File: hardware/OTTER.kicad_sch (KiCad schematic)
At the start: 0 parts

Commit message: starting layout
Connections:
- no-connect marks 15 -> 16
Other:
- sheet PMOD Connector ports: added JA4; removed none
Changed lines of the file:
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@@
+	)
+	(no_connect
+		(at 97.79 73.66)
 	)
 	(no_connect
@@
 	(wire
 		(pts
-			(xy 139.7 27.94) (xy 157.48 27.94)
+			(xy 78.74 39.37) (xy 93.98 39.37)
 		)
 		(stroke
@@
 	(wire
 		(pts
-			(xy 78.74 39.37) (xy 93.98 39.37)
+			(xy 78.74 48.26) (xy 93.98 48.26)
 		)
 		(stroke
@@
 	(wire
 		(pts
-			(xy 78.74 48.26) (xy 93.98 48.26)
+			(xy 139.7 30.48) (xy 157.48 30.48)
 		)
 		(stroke
@@
 	(wire
 		(pts
-			(xy 139.7 30.48) (xy 157.48 30.48)
+			(xy 78.74 29.21) (xy 93.98 29.21)
 		)
 		(stroke
@@
 	(wire
 		(pts
-			(xy 78.74 29.21) (xy 93.98 29.21)
+			(xy 139.7 35.56) (xy 157.48 35.56)
 		)
 		(stroke
@@
 	(wire
 		(pts
-			(xy 139.7 35.56) (xy 157.48 35.56)
+			(xy 78.74 53.34) (xy 93.98 53.34)
 		)
 		(stroke
@@
 	(wire
 		(pts
-			(xy 78.74 53.34) (xy 93.98 53.34)
+			(xy 78.74 31.75) (xy 93.98 31.75)
 		)
 		(stroke
@@
 	(wire
 		(pts
-			(xy 78.74 31.75) (xy 93.98 31.75)
+			(xy 139.7 38.1) (xy 157.48 38.1)
 		)
 		(stroke
@@
 	(wire
 		(pts
-			(xy 139.7 38.1) (xy 157.48 38.1)
+			(xy 78.74 55.88) (xy 93.98 55.88)
 		)
 		(stroke
@@
 	(wire
 		(pts
-			(xy 78.74 55.88) (xy 93.98 55.88)
+			(xy 78.74 34.29) (xy 93.98 34.29)
 		)
 		(stroke
@@
 	(wire
 		(pts
-			(xy 78.74 34.29) (xy 93.98 34.29)
+			(xy 78.74 36.83) (xy 93.98 36.83)
 		)
 		(stroke
@@
 	(wire
 		(pts
-			(xy 78.74 36.83) (xy 93.98 36.83)
+			(xy 78.74 44.45) (xy 93.98 44.45)
 		)
 		(stroke
@@
 	(wire
 		(pts
-			(xy 78.74 44.45) (xy 93.98 44.45)
+			(xy 139.7 33.02) (xy 157.48 33.02)
 		)
 		(stroke
@@
 	(wire
 		(pts
-			(xy 139.7 33.02) (xy 157.48 33.02)
+			(xy 139.7 40.64) (xy 157.48 40.64)
 		)
 		(stroke
@@
 		)
 		(pin "JD1" output
-			(at 139.7 27.94 0)
+			(at 139.7 40.64 0)
 			(effects
 				(font
@@
 		(pin "JD9" output
 			(at 93.98 31.75 180)
+			(effects
+				(font
+					(size 1.27 1.27)
+				)
+				(justify left)
+			)
+		)
+		(pin "JA4" output
+			(at 97.79 73.66 270)
 			(effects
 				(font
@@
 		)
 		(pin "CS" input
-			(at 157.48 27.94 180)
-			(effects
-				(font
+			(at 157.48 40.64 180)
+			(effects
+				(font

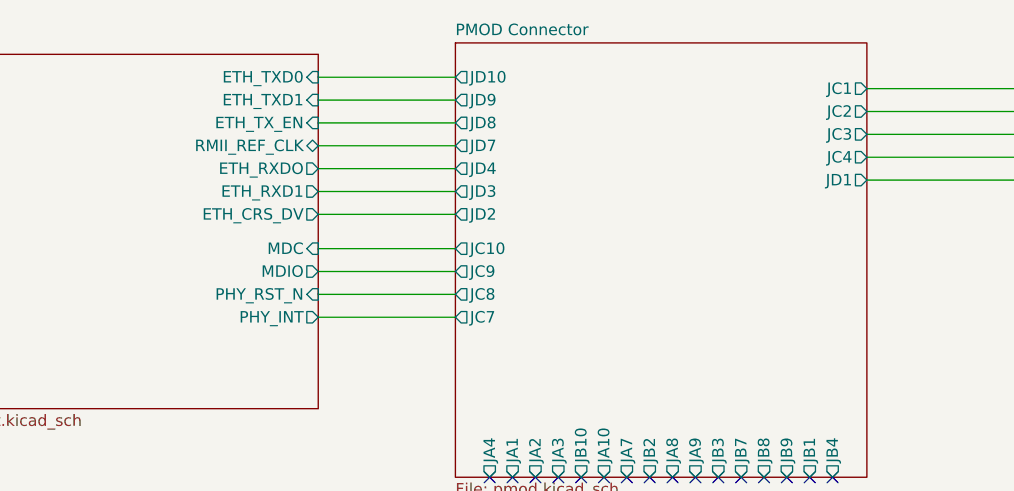
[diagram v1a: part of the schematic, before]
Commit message: changed pinout to match trs-star. also added resistors for spi
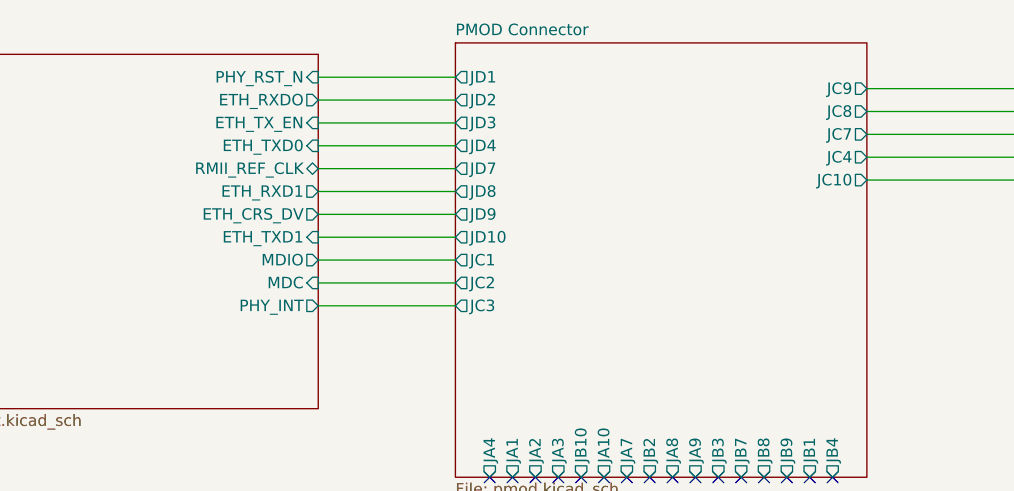
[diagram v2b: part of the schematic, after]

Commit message: most of layout is done, only have single ended highspeed signals left. mika pleaaaaaaaaaaaaaaaaaseeeeeeee review :beg:
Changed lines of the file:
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@@
-	(wire
-		(pts
-			(xy 139.7 35.56) (xy 157.48 35.56)
-		)
-		(stroke
-			(width 0)
-			(type default)
-		)
-	)
 	(wire
 		(pts
@@
 	(wire
 		(pts
-			(xy 78.74 49.53) (xy 93.98 49.53)
+			(xy 139.7 30.48) (xy 157.48 30.48)
+		)
+		(stroke
+			(width 0)
+			(type default)
+		)
+	)
+	(wire
+		(pts
+			(xy 78.74 36.83) (xy 93.98 36.83)
+		)
+		(stroke
+			(width 0)
+			(type default)
+		)
+	)
+	(wire
+		(pts
+			(xy 78.74 54.61) (xy 93.98 54.61)
+		)
+		(stroke
+			(width 0)
+			(type default)
+		)
+	)
+	(wire
+		(pts
+			(xy 78.74 31.75) (xy 93.98 31.75)
 		)
 		(stroke
@@
 	(wire
 		(pts
-			(xy 78.74 36.83) (xy 93.98 36.83)
+			(xy 139.7 33.02) (xy 157.48 33.02)
 		)
 		(stroke
@@
 	(wire
 		(pts
-			(xy 78.74 54.61) (xy 93.98 54.61)
-		)
-		(stroke
-			(width 0)
-			(type default)
-		)
-	)
-	(wire
-		(pts
-			(xy 78.74 31.75) (xy 93.98 31.75)
-		)
-		(stroke
-			(width 0)
-			(type default)
-		)
-	)
-	(wire
-		(pts
-			(xy 139.7 33.02) (xy 157.48 33.02)
-		)
-		(stroke
-			(width 0)
-			(type default)
-		)
-	)
-	(wire
-		(pts
-			(xy 139.7 30.48) (xy 157.48 30.48)
+			(xy 139.7 35.56) (xy 157.48 35.56)
 		)
 		(stroke
@@
 	(wire
 		(pts
-			(xy 78.74 52.07) (xy 93.98 52.07)
+			(xy 139.7 38.1) (xy 157.48 38.1)
 		)
 		(stroke
@@
 	(wire
 		(pts
-			(xy 139.7 38.1) (xy 157.48 38.1)
+			(xy 78.74 49.53) (xy 93.98 49.53)
+		)
+		(stroke
+			(width 0)
+			(type default)
+		)
+	)
+	(wire
+		(pts
+			(xy 78.74 52.07) (xy 93.98 52.07)
 		)
 		(stroke
@@
 		)
 		(pin "JC1" output
+			(at 139.7 40.64 0)
+			(effects
+				(font
+					(size 1.27 1.27)
+				)
+				(justify right)
+			)
+		)
+		(pin "JC10" output
+			(at 93.98 52.07 180)
+			(effects
+				(font
+					(size 1.27 1.27)
+				)
+				(justify left)
+			)
+		)
+		(pin "JC2" output
+			(at 139.7 30.48 0)
+			(effects
+				(font
+					(size 1.27 1.27)
+				)
+				(justify right)
+			)
+		)
+		(pin "JC3" output
+			(at 139.7 38.1 0)
+			(effects
+				(font
+					(size 1.27 1.27)
+				)
+				(justify right)
+			)
+		)
+		(pin "JC4" output
+			(at 139.7 35.56 0)
+			(effects
+				(font
+					(size 1.27 1.27)
+				)
+				(justify right)
+			)
+		)
+		(pin "JC7" output
+			(at 139.7 33.02 0)
+			(effects
+				(font
+					(size 1.27 1.27)
+				)
+				(justify right)
+			)
+		)
+		(pin "JC8" output
+			(at 93.98 54.61 180)
+			(effects
+				(font
+					(size 1.27 1.27)
+				)
+				(justify left)
+			)
+		)
+		(pin "JC9" output
 			(at 93.98 49.53 180)
 			(effects
@@
 			)
 		)
-		(pin "JC10" output
-			(at 139.7 40.64 0)
-			(effects
-				(font
-					(size 1.27 1.27)
-				)
-				(justify right)
-			)
-		)
-		(pin "JC2" output
-			(at 93.98 52.07 180)
-			(effects
-				(font
-					(size 1.27 1.27)
-				)
-				(justify left)
-			)
-		)
-		(pin "JC3" output
-			(at 93.98 54.61 180)
-			(effects
-				(font
-					(size 1.27 1.27)
-				)
-				(justify left)
-			)
-		)
-		(pin "JC4" output
-			(at 139.7 38.1 0)
-			(effects
-				(font
-					(size 1.27 1.27)
-				)
-				(justify right)
-			)
-		)
-		(pin "JC7" output
-			(at 139.7 35.56 0)
-			(effects
-				(font
-					(size 1.27 1.27)
-				)
-				(justify right)
-			)
-		)
-		(pin "JC8" output
-			(at 139.7 33.02 0)
-			(effects
-				(font
-					(size 1.27 1.27)
-				)
-				(justify right)
-			)
-		)
-		(pin "JC9" output
-			(at 139.7 30.48 0)
-			(effects
-				(font
-					(size 1.27 1.27)
-				)
-				(justify right)
-			)
-		)
